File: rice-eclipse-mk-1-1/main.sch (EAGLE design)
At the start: 59 parts, among them IC1 LM7705, U1 LM1084ISX-5.0/NOPB, U2 THS4531IDRD8-M, U3 THS4531IDRD8-M, U4 THS4531IDRD8-M, U5 THS4531IDRD8-M, X1 2540-5

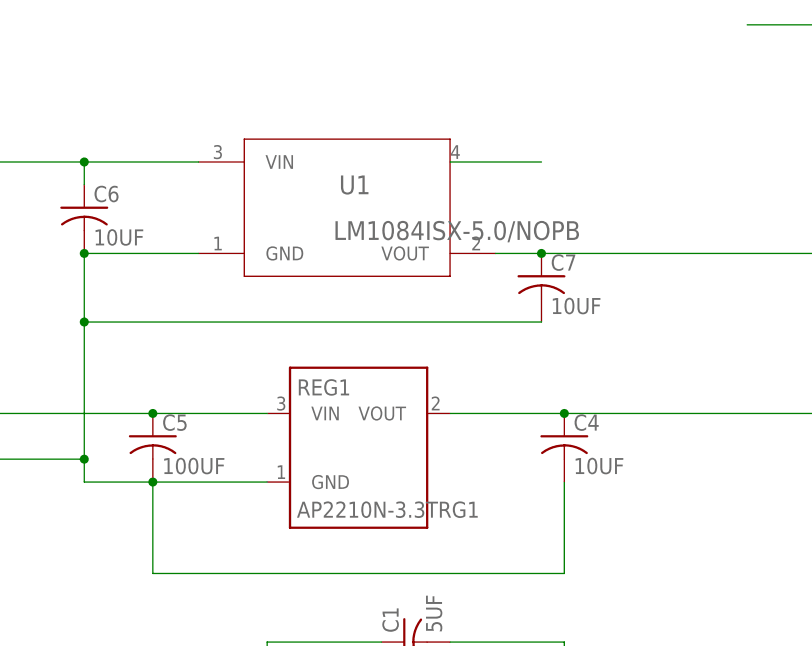
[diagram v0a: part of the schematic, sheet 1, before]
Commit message: Cleaned up placement on the board. Router scares me.
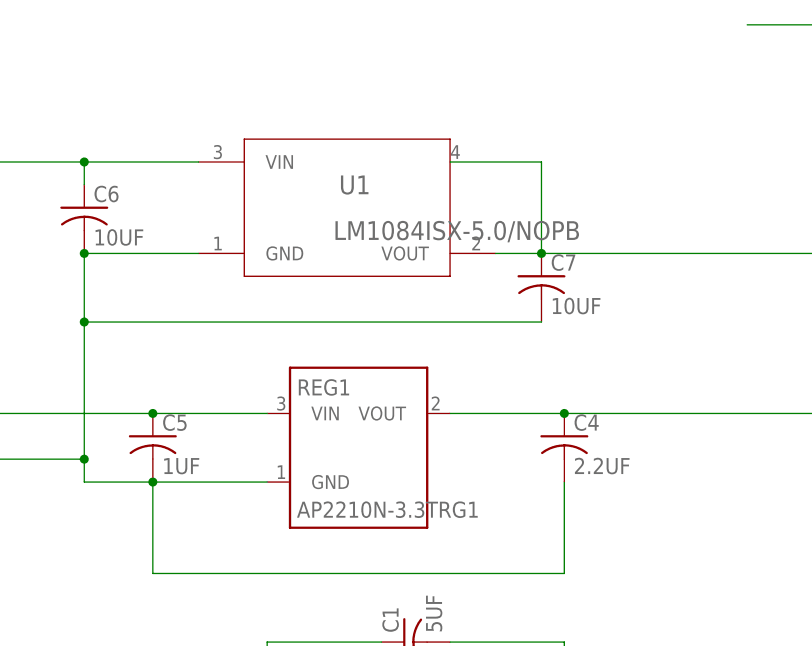
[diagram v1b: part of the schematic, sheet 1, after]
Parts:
- removed SH1: SHORTT5, shorts:SHORTT5
- C4: value 10UF -> 2.2UF; device rcl:C-US025-050X050 -> rcl:C-USC0603
- C5: value 100UF -> 1UF; device rcl:C-US025-050X050 -> rcl:C-USC0603
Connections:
- removed net N$4: U1.4
- removed net TEST_NET_1: SH1.P$1
- removed net TEST_NET_2: SH1.P$2
- new net N$11: X4-5.SK
- net +5V: now also U1.4
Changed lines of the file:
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@@
 <part name="C3" library="resistor" library_urn="urn:adsk.eagle:library:348" deviceset="C-US" device="C0603" package3d_urn="urn:adsk.eagle:package:26138/1" value="1UF"/>
 <part name="REG1" library="diodes-extra" deviceset="AP2210N-3.3TRG1" device=""/>
-<part name="C4" library="rcl" library_urn="urn:adsk.eagle:library:334" deviceset="C-US" device="025-050X050" package3d_urn="urn:adsk.eagle:package:23633/1" value="10UF"/>
-<part name="C5" library="rcl" library_urn="urn:adsk.eagle:library:334" deviceset="C-US" device="025-050X050" package3d_urn="urn:adsk.eagle:package:23633/1" value="100UF"/>
+<part name="C4" library="rcl" library_urn="urn:adsk.eagle:library:334" deviceset="C-US" device="C0603" package3d_urn="urn:adsk.eagle:package:23616/2" value="2.2UF"/>
+<part name="C5" library="rcl" library_urn="urn:adsk.eagle:library:334" deviceset="C-US" device="C0603" package3d_urn="urn:adsk.eagle:package:23616/2" value="1UF"/>
 <part name="U1" library="texas-extra" deviceset="LM1084ISX-5.0/NOPB" device=""/>
 <part name="C6" library="rcl" library_urn="urn:adsk.eagle:library:334" deviceset="C-US" device="025-050X050" package3d_urn="urn:adsk.eagle:package:23633/1" value="10UF"/>
@@
 <part name="FRAME5" library="frames" library_urn="urn:adsk.eagle:library:229" deviceset="A4L-LOC" device=""/>
 <part name="FRAME6" library="frames" library_urn="urn:adsk.eagle:library:229" deviceset="A4L-LOC" device=""/>
-<part name="SH1" library="shorts" deviceset="SHORT" device="T5"/>
 <part name="FRAME1" library="frames" library_urn="urn:adsk.eagle:library:229" deviceset="A4L-LOC" device=""/>
 <part name="FRAME7" library="frames" library_urn="urn:adsk.eagle:library:229" deviceset="A4L-LOC" device=""/>
@@
 <label x="213.36" y="111.76" size="1.778" layer="95"/>
 <pinref part="U1" gate="A" pin="VOUT"/>
-<wire x1="165.1" y1="111.76" x2="170.18" y2="111.76" width="0.1524" layer="91"/>
 <pinref part="C7" gate="G$1" pin="1"/>
 <wire x1="170.18" y1="111.76" x2="213.36" y2="111.76" width="0.1524" layer="91"/>
 <junction x="170.18" y="111.76"/>
+<wire x1="165.1" y1="111.76" x2="170.18" y2="111.76" width="0.1524" layer="91"/>
+<pinref part="U1" gate="A" pin="4"/>
+<wire x1="160.02" y1="121.92" x2="170.18" y2="121.92" width="0.1524" layer="91"/>
+<wire x1="170.18" y1="121.92" x2="170.18" y2="111.76" width="0.1524" layer="91"/>
 </segment>
 <segment>
@@
 </segment>
 </net>
-<net name="N$4" class="0">
-<segment>
-<pinref part="U1" gate="A" pin="4"/>
-<wire x1="160.02" y1="121.92" x2="170.18" y2="121.92" width="0.1524" layer="91"/>
-</segment>
-</net>
 </nets>
 </sheet>
@@
 A schematic for amplifying signals from the load cells. Additional Level-Shifting circuits may be necessary, this is important as well.</description>
 <plain>
-<text x="33.02" y="154.94" size="1.778" layer="97">TODO: Bypass caps</text>
-<text x="27.94" y="119.38" size="1.778" layer="97">Need to add variable gain using potentiometer.</text>
 <text x="134.62" y="157.48" size="1.778" layer="97">TODO: Bypass caps</text>
 <text x="129.54" y="121.92" size="1.778" layer="97">Need to add variable gain using potentiometer.</text>
@@
 <net name="N$11" class="0">
 <segment>
-<wire x1="30.48" y1="81.28" x2="38.1" y2="81.28" width="0.1524" layer="91"/>
+<wire x1="27.94" y1="81.28" x2="38.1" y2="81.28" width="0.1524" layer="91"/>
 <label x="38.1" y="81.28" size="1.778" layer="95"/>
+<pinref part="X4" gate="-5" pin="SK"/>
 </segment>
 </net>
@@
 </plain>
 <instances>
-<instance part="SH1" gate="G$1" x="93.98" y="68.58"/>
 </instances>
 <busses>
 </busses>
 <nets>
-<net name="TEST_NET_1" class="0">
-<segment>
-<wire x1="35.56" y1="68.58" x2="91.44" y2="68.58" width="0.1524" layer="91"/>
-<label x="83.82" y="63.5" size="1.778" layer="95"/>
-<pinref part="SH1" gate="G$1" pin="P$1"/>
-</segment>
-</net>
-<net name="TEST_NET_2" class="0">
-<segment>
-<wire x1="96.52" y1="68.58" x2="157.48" y2="68.58" width="0.1524" layer="91"/>
-<label x="101.6" y="71.12" size="1.778" layer="95"/>
-<pinref part="SH1" gate="G$1" pin="P$2"/>
-</segment>
-</net>
 </nets>
 </sheet>

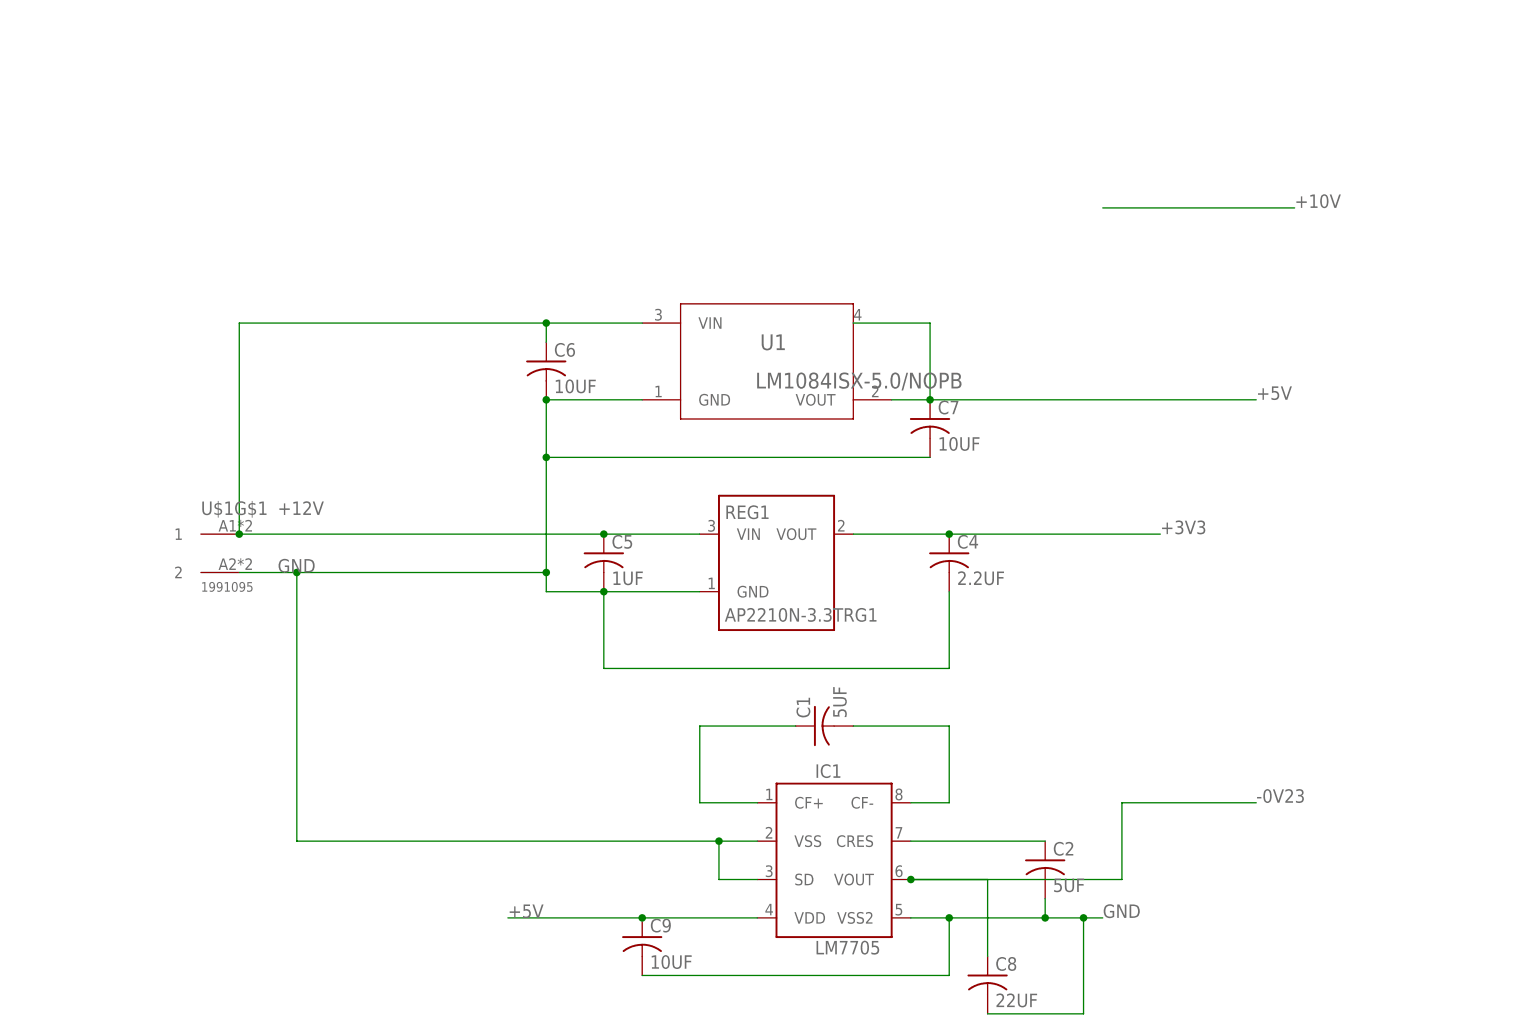
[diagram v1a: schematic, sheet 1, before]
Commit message: Added a new 4-pin signal connector. Also modified board.
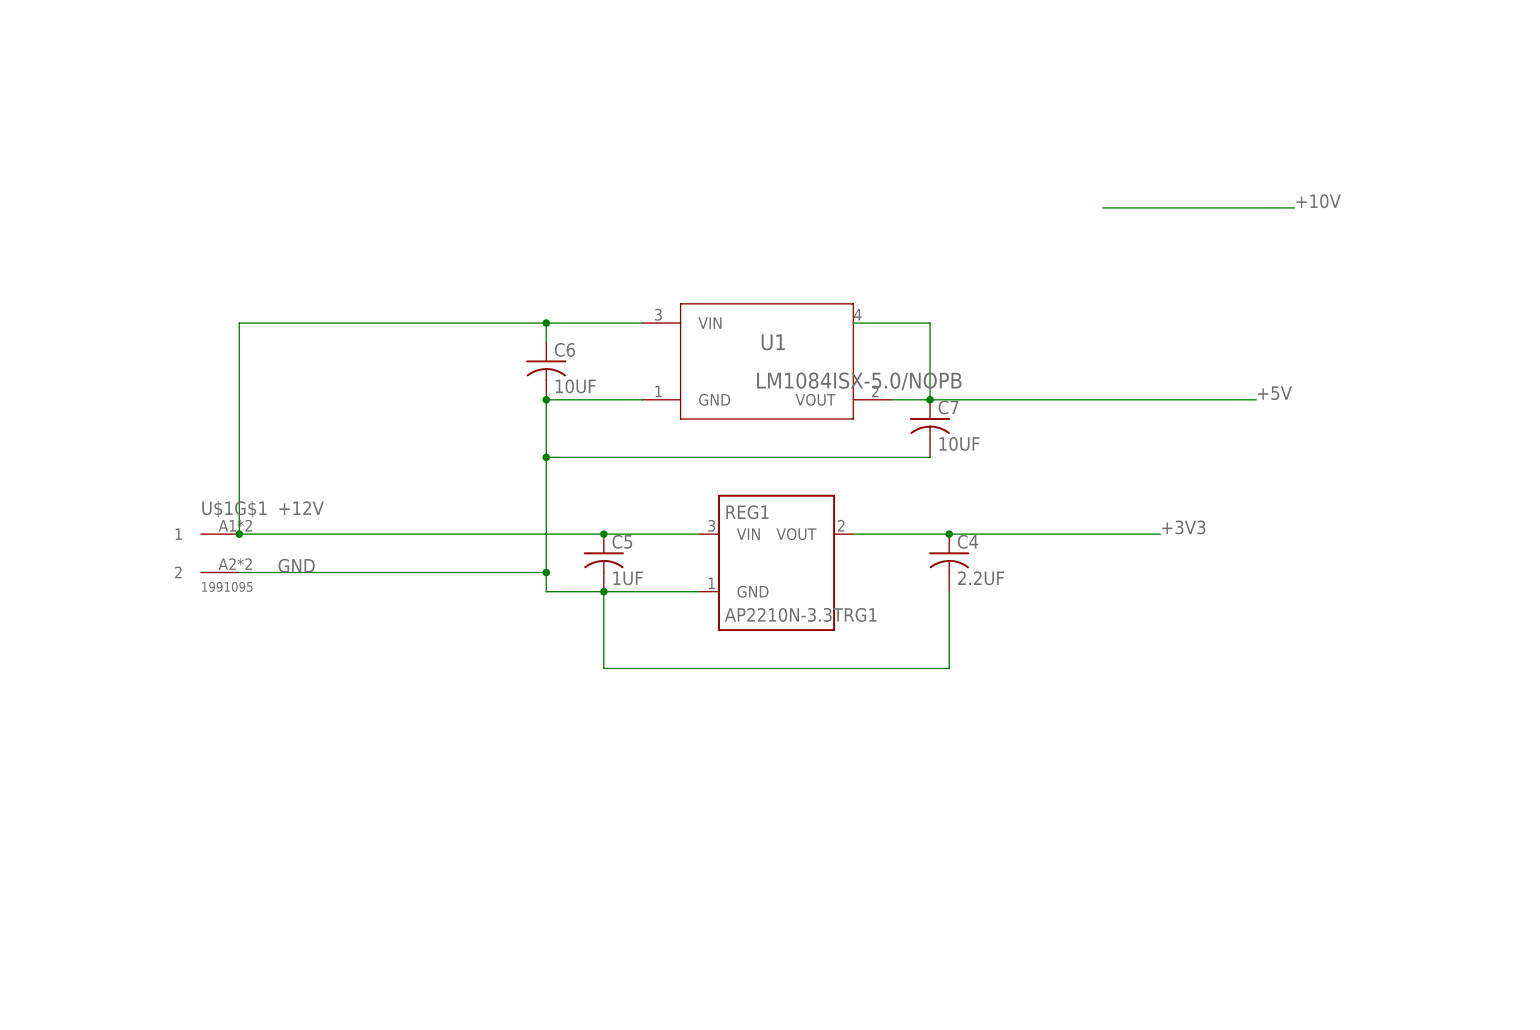
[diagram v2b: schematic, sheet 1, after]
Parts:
- removed C1, C2: 5UF, rcl:C-USC0603
- removed C8: 22UF, rcl:C-USC0603
- removed C9: 10UF, rcl:C-USC0603
- removed IC1: LM7705, texas-extra:LM7705
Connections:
- removed net -0V23: C10.2, C11.2, C12.2, C13.2, C8.1, IC1.VOUT, U2.VS-, U3.VS-, U4.VS-, U5.VS-
- removed net AGND: ADC1.AGND, C3.2
- removed net DGND: ADC1.DGND
- removed net N$1: C1.1, IC1.CF+
- removed net N$2: C1.2, IC1.CF-
- removed net N$3: C2.1, IC1.CRES
- net +5V: no longer C9.1, IC1.VDD
- net GND: now also ADC1.AGND, ADC1.DGND, C10.2, C11.2, C12.2, C13.2, C3.2, U2.VS-, U3.VS-, U4.VS-, U5.VS-; no longer C2.2, C8.2, C9.2, IC1.SD, IC1.VSS, IC1.VSS2
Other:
- note removed: "Need to add variable gain using potentiometer."
- note removed: "TODO: Bypass caps"
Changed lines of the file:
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@@
 <part name="FRAME7" library="frames" library_urn="urn:adsk.eagle:library:229" deviceset="A4L-LOC" device=""/>
 <part name="FRAME8" library="frames" library_urn="urn:adsk.eagle:library:229" deviceset="A4L-LOC" device=""/>
-<part name="IC1" library="texas-extra" deviceset="LM7705" device=""/>
-<part name="C1" library="rcl" library_urn="urn:adsk.eagle:library:334" deviceset="C-US" device="C0603" package3d_urn="urn:adsk.eagle:package:23616/2" value="5UF"/>
-<part name="C2" library="rcl" library_urn="urn:adsk.eagle:library:334" deviceset="C-US" device="C0603" package3d_urn="urn:adsk.eagle:package:23616/2" value="5UF"/>
-<part name="C8" library="rcl" library_urn="urn:adsk.eagle:library:334" deviceset="C-US" device="C0603" package3d_urn="urn:adsk.eagle:package:23616/2" value="22UF"/>
-<part name="C9" library="rcl" library_urn="urn:adsk.eagle:library:334" deviceset="C-US" device="C0603" package3d_urn="urn:adsk.eagle:package:23616/2" value="10UF"/>
 <part name="FRAME9" library="frames" library_urn="urn:adsk.eagle:library:229" deviceset="A4L-LOC" device=""/>
 <part name="X1" library="con-3m" library_urn="urn:adsk.eagle:library:119" deviceset="2540-" device="5" package3d_urn="urn:adsk.eagle:package:5588/1"/>
@@
 <attribute name="SHEET" x="230.505" y="5.08" size="2.54" layer="94"/>
 </instance>
-<instance part="IC1" gate="G$1" x="157.48" y="50.8"/>
-<instance part="C1" gate="G$1" x="154.94" y="68.58" rot="R90"/>
-<instance part="C2" gate="G$1" x="185.42" y="50.8"/>
-<instance part="C8" gate="G$1" x="177.8" y="35.56"/>
-<instance part="C9" gate="G$1" x="132.08" y="40.64"/>
 <instance part="U$1" gate="G$1" x="78.74" y="93.98"/>
 <instance part="U$1" gate="G$2" x="78.74" y="88.9"/>
@@
 <segment>
 <label x="83.82" y="88.9" size="1.778" layer="95"/>
-<wire x1="119.38" y1="88.9" x2="86.36" y2="88.9" width="0.1524" layer="91"/>
-<wire x1="86.36" y1="88.9" x2="78.74" y2="88.9" width="0.1524" layer="91"/>
+<wire x1="119.38" y1="88.9" x2="78.74" y2="88.9" width="0.1524" layer="91"/>
 <pinref part="U1" gate="A" pin="GND"/>
 <wire x1="132.08" y1="111.76" x2="119.38" y2="111.76" width="0.1524" layer="91"/>
@@
 <wire x1="170.18" y1="104.14" x2="119.38" y2="104.14" width="0.1524" layer="91"/>
 <junction x="119.38" y="104.14"/>
-<pinref part="IC1" gate="G$1" pin="VSS"/>
-<wire x1="147.32" y1="53.34" x2="142.24" y2="53.34" width="0.1524" layer="91"/>
-<wire x1="142.24" y1="53.34" x2="86.36" y2="53.34" width="0.1524" layer="91"/>
-<wire x1="86.36" y1="53.34" x2="86.36" y2="88.9" width="0.1524" layer="91"/>
-<junction x="86.36" y="88.9"/>
-<pinref part="IC1" gate="G$1" pin="SD"/>
-<wire x1="147.32" y1="48.26" x2="142.24" y2="48.26" width="0.1524" layer="91"/>
-<wire x1="142.24" y1="48.26" x2="142.24" y2="53.34" width="0.1524" layer="91"/>
-<junction x="142.24" y="53.34"/>
 <pinref part="U$1" gate="G$2" pin="2"/>
 <wire x1="119.38" y1="88.9" x2="119.38" y2="86.36" width="0.1524" layer="91"/>
@@
 <wire x1="172.72" y1="76.2" x2="172.72" y2="86.36" width="0.1524" layer="91"/>
 <wire x1="119.38" y1="86.36" x2="127" y2="86.36" width="0.1524" layer="91"/>
-</segment>
-<segment>
-<pinref part="IC1" gate="G$1" pin="VSS2"/>
-<wire x1="167.64" y1="43.18" x2="172.72" y2="43.18" width="0.1524" layer="91"/>
-<label x="193.04" y="43.18" size="1.778" layer="95"/>
-<pinref part="C9" gate="G$1" pin="2"/>
-<wire x1="172.72" y1="43.18" x2="185.42" y2="43.18" width="0.1524" layer="91"/>
-<wire x1="185.42" y1="43.18" x2="190.5" y2="43.18" width="0.1524" layer="91"/>
-<wire x1="190.5" y1="43.18" x2="193.04" y2="43.18" width="0.1524" layer="91"/>
-<wire x1="132.08" y1="35.56" x2="172.72" y2="35.56" width="0.1524" layer="91"/>
-<wire x1="172.72" y1="35.56" x2="172.72" y2="43.18" width="0.1524" layer="91"/>
-<junction x="172.72" y="43.18"/>
-<pinref part="C2" gate="G$1" pin="2"/>
-<wire x1="185.42" y1="45.72" x2="185.42" y2="43.18" width="0.1524" layer="91"/>
-<junction x="185.42" y="43.18"/>
-<pinref part="C8" gate="G$1" pin="2"/>
-<wire x1="177.8" y1="30.48" x2="190.5" y2="30.48" width="0.1524" layer="91"/>
-<wire x1="190.5" y1="30.48" x2="190.5" y2="43.18" width="0.1524" layer="91"/>
-<junction x="190.5" y="43.18"/>
 </segment>
 </net>
@@
 <wire x1="170.18" y1="121.92" x2="170.18" y2="111.76" width="0.1524" layer="91"/>
 </segment>
-<segment>
-<pinref part="IC1" gate="G$1" pin="VDD"/>
-<pinref part="C9" gate="G$1" pin="1"/>
-<wire x1="147.32" y1="43.18" x2="132.08" y2="43.18" width="0.1524" layer="91"/>
-<wire x1="132.08" y1="43.18" x2="114.3" y2="43.18" width="0.1524" layer="91"/>
-<junction x="132.08" y="43.18"/>
-<label x="114.3" y="43.18" size="1.778" layer="95"/>
-</segment>
-</net>
-<net name="-0V23" class="0">
-<segment>
-<wire x1="195.58" y1="58.42" x2="213.36" y2="58.42" width="0.1524" layer="91"/>
-<label x="213.36" y="58.42" size="1.778" layer="95"/>
-<pinref part="IC1" gate="G$1" pin="VOUT"/>
-<pinref part="C8" gate="G$1" pin="1"/>
-<wire x1="167.64" y1="48.26" x2="177.8" y2="48.26" width="0.1524" layer="91"/>
-<wire x1="177.8" y1="48.26" x2="177.8" y2="38.1" width="0.1524" layer="91"/>
-<wire x1="167.64" y1="48.26" x2="195.58" y2="48.26" width="0.1524" layer="91"/>
-<wire x1="195.58" y1="48.26" x2="195.58" y2="58.42" width="0.1524" layer="91"/>
-<junction x="167.64" y="48.26"/>
-</segment>
 </net>
 <net name="+10V" class="0">
@@
 <wire x1="193.04" y1="137.16" x2="218.44" y2="137.16" width="0.1524" layer="91"/>
 <label x="218.44" y="137.16" size="1.778" layer="95"/>
-</segment>
-</net>
-<net name="N$1" class="0">
-<segment>
-<pinref part="C1" gate="G$1" pin="1"/>
-<wire x1="152.4" y1="68.58" x2="139.7" y2="68.58" width="0.1524" layer="91"/>
-<wire x1="139.7" y1="68.58" x2="139.7" y2="58.42" width="0.1524" layer="91"/>
-<pinref part="IC1" gate="G$1" pin="CF+"/>
-<wire x1="139.7" y1="58.42" x2="147.32" y2="58.42" width="0.1524" layer="91"/>
-</segment>
-</net>
-<net name="N$2" class="0">
-<segment>
-<pinref part="C1" gate="G$1" pin="2"/>
-<wire x1="160.02" y1="68.58" x2="172.72" y2="68.58" width="0.1524" layer="91"/>
-<wire x1="172.72" y1="68.58" x2="172.72" y2="58.42" width="0.1524" layer="91"/>
-<pinref part="IC1" gate="G$1" pin="CF-"/>
-<wire x1="172.72" y1="58.42" x2="167.64" y2="58.42" width="0.1524" layer="91"/>
-</segment>
-</net>
-<net name="N$3" class="0">
-<segment>
-<pinref part="IC1" gate="G$1" pin="CRES"/>
-<pinref part="C2" gate="G$1" pin="1"/>
-<wire x1="167.64" y1="53.34" x2="185.42" y2="53.34" width="0.1524" layer="91"/>
 </segment>
 </net>
@@
 A schematic for amplifying signals from the load cells. Additional Level-Shifting circuits may be necessary, this is important as well.</description>
 <plain>
-<text x="134.62" y="157.48" size="1.778" layer="97">TODO: Bypass caps</text>
-<text x="129.54" y="121.92" size="1.778" layer="97">Need to add variable gain using potentiometer.</text>
-<text x="30.48" y="76.2" size="1.778" layer="97">TODO: Bypass caps</text>
-<text x="25.4" y="40.64" size="1.778" layer="97">Need to add variable gain using potentiometer.</text>
-<text x="137.16" y="78.74" size="1.778" layer="97">TODO: Bypass caps</text>
-<text x="132.08" y="43.18" size="1.778" layer="97">Need to add variable gain using potentiometer.</text>
 </plain>
 <instances>
@@
 </busses>
 <nets>
-<net name="-0V23" class="0">
+<net name="GND" class="0">
 <segment>
 <pinref part="C10" gate="G$1" pin="2"/>
@@
 </segment>
 </net>
-<net name="DGND" class="0">
-<segment>
-<wire x1="53.34" y1="63.5" x2="53.34" y2="73.66" width="0.1524" layer="91"/>
-<pinref part="ADC1" gate="P" pin="DGND"/>
-<wire x1="53.34" y1="73.66" x2="58.42" y2="73.66" width="0.1524" layer="91"/>
-<label x="53.34" y="63.5" size="1.778" layer="95"/>
-</segment>
-</net>
 <net name="SCLK" class="0">
 <segment>
@@
 </segment>
 </net>
-<net name="AGND" class="0">
+<net name="GND" class="0">
 <segment>
 <pinref part="ADC1" gate="P" pin="AGND"/>
@@
 <junction x="106.68" y="99.06"/>
 </segment>
-</net>
+<segment>
+<wire x1="53.34" y1="63.5" x2="53.34" y2="73.66" width="0.1524" layer="91"/>
+<pinref part="ADC1" gate="P" pin="DGND"/>
+<wire x1="53.34" y1="73.66" x2="58.42" y2="73.66" width="0.1524" layer="91"/>
+<label x="53.34" y="63.5" size="1.778" layer="95"/>
+</segment>
+</net>
